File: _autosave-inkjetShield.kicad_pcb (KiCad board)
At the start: 2 copper layers, 1 part, among them U1 Teensy4.1

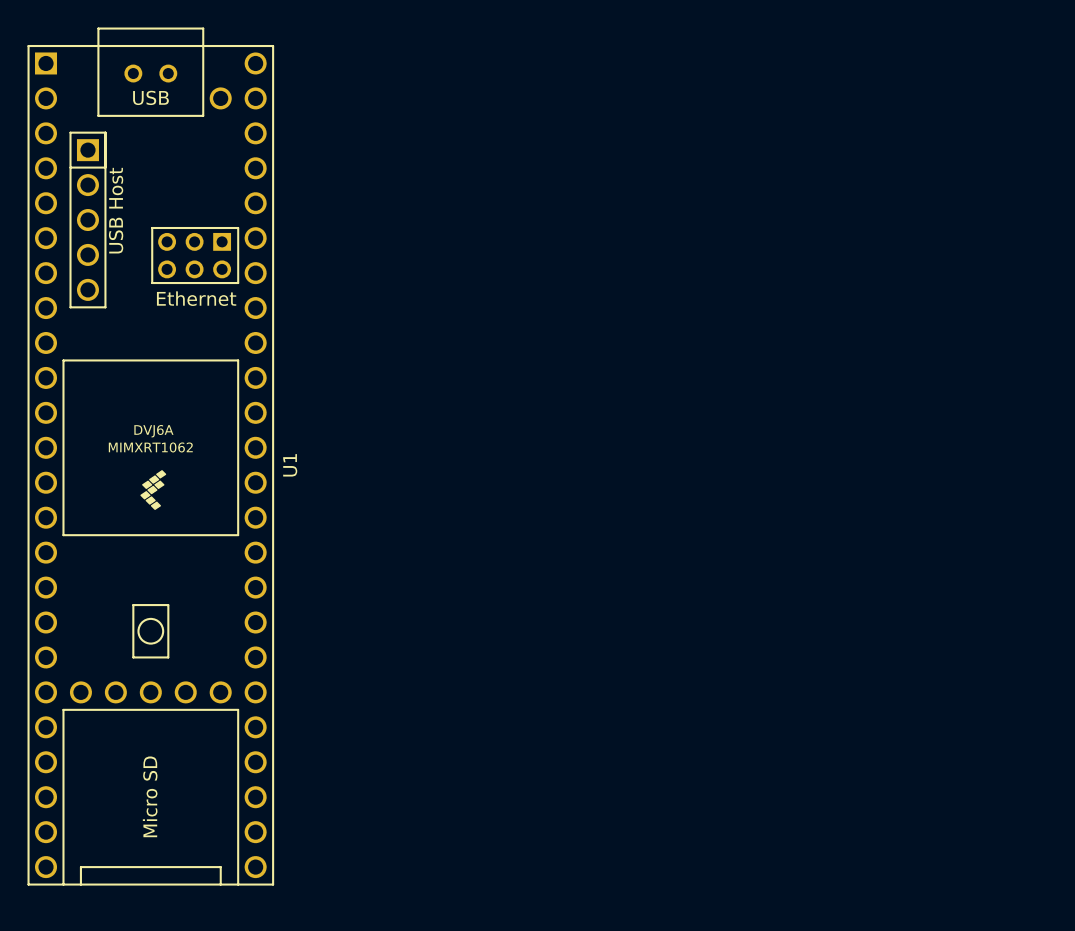
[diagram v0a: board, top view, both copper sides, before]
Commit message: identified target components and updated schematic
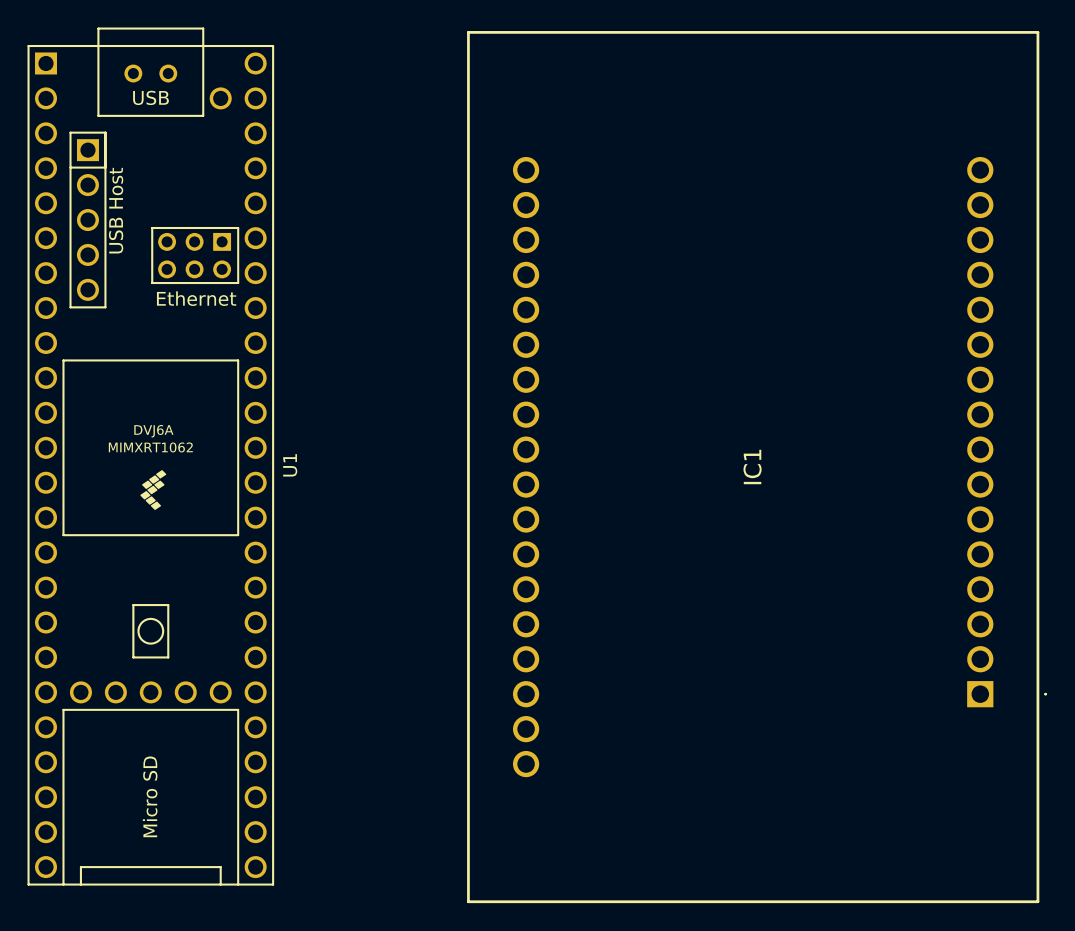
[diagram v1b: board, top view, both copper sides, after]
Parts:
- added IC1: MP108FD, custom:MP108FD, F.Cu at (142.1, 104.8)
